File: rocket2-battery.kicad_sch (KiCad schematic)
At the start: 14 parts, among them J1 Conn_01x07, P1 PAD_SMD, P2 PAD_SMD, P3 PAD_SMD, P4 PAD_SMD

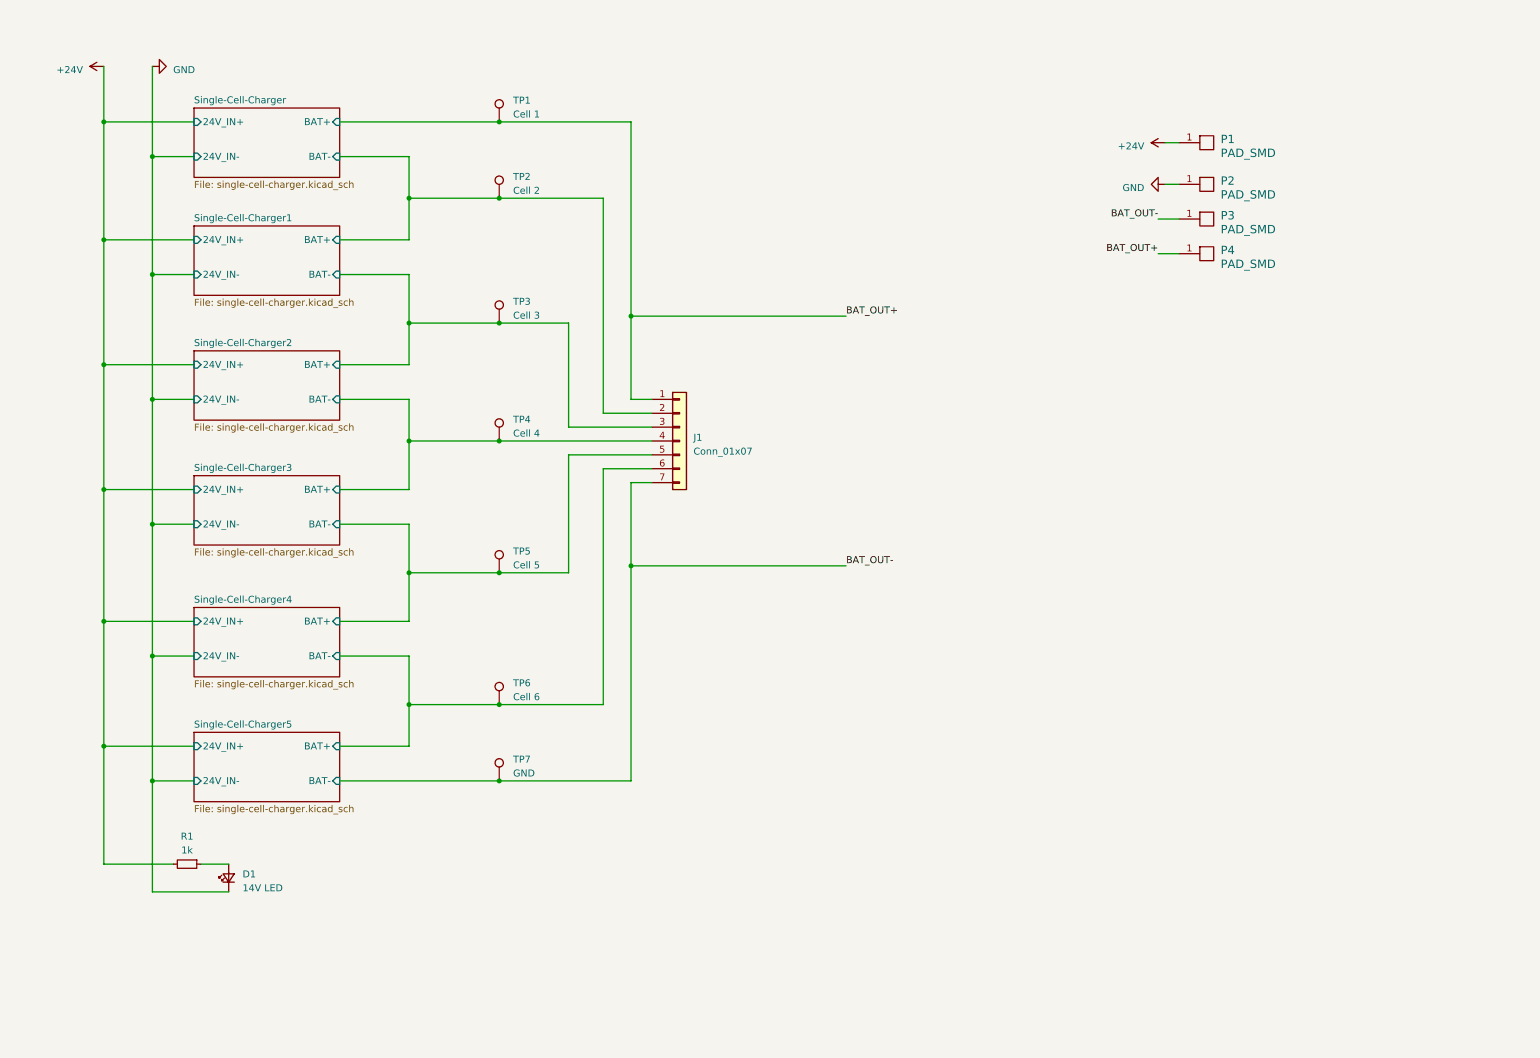
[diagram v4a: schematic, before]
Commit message: Updated schematic with symbols and footprints
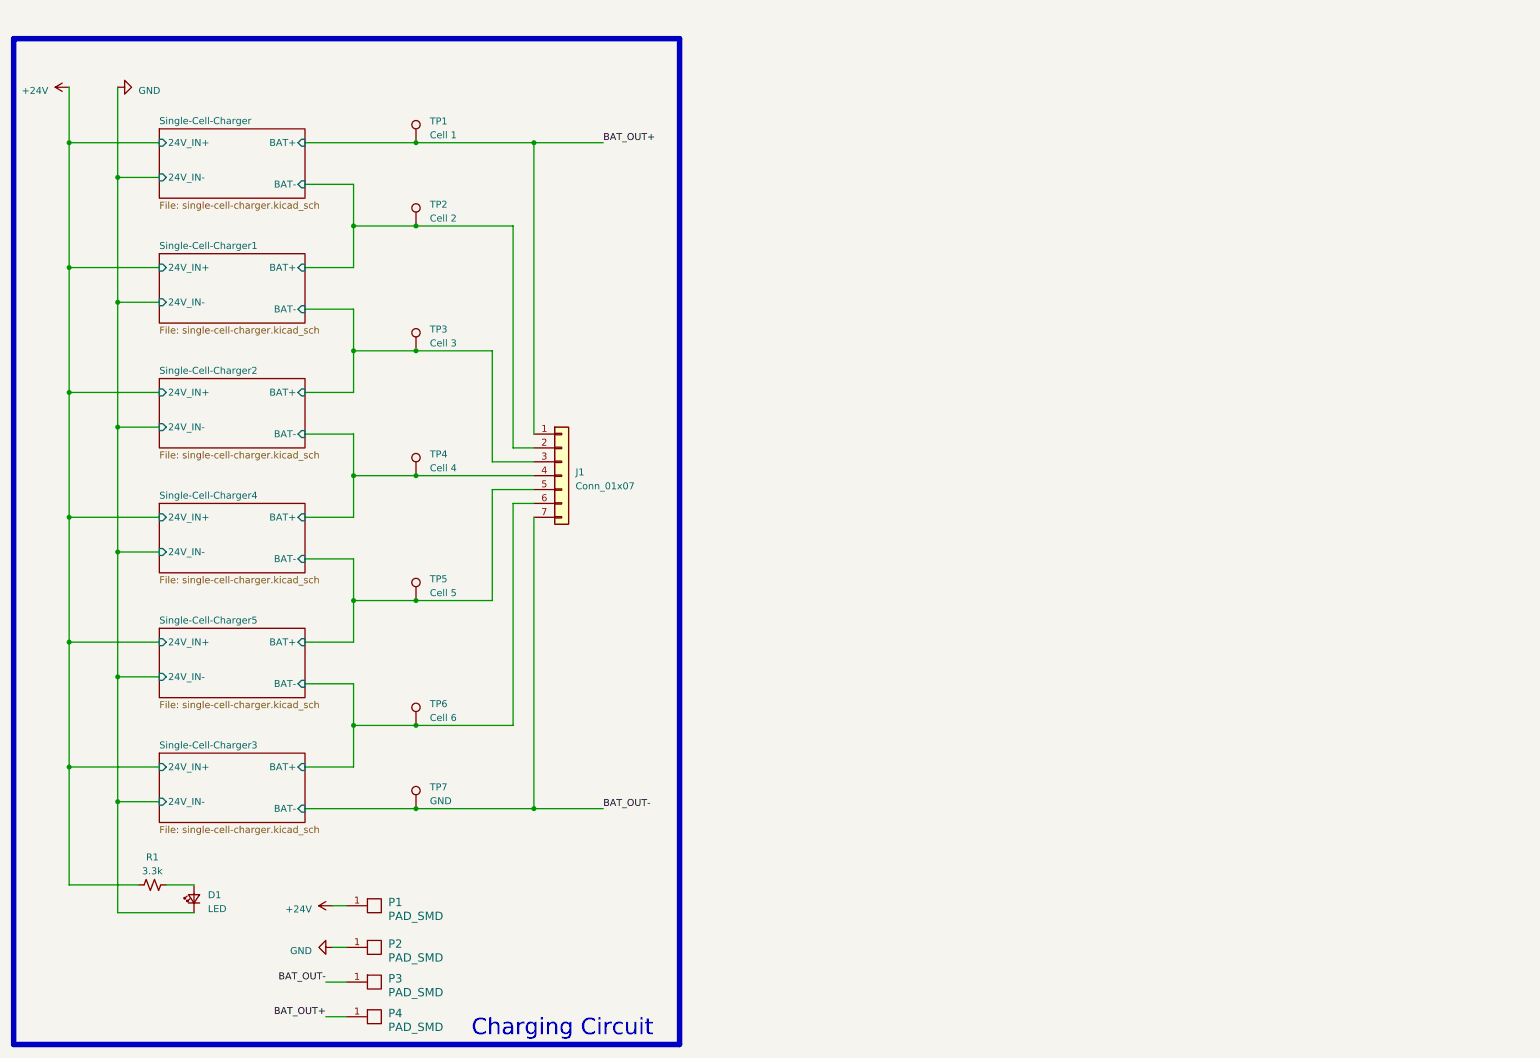
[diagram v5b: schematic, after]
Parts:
- removed R1: 1k, symbol Device:R_Small
- added R1: 3.3k, Resistor_SMD:R_0603_1608Metric_Pad0.98x0.95mm_HandSolder, symbol Device:R_Small_US
- D1: value 14V LED -> LED; footprint LED_THT:LED_D5.0mm -> LED_SMD:LED_0603_1608Metric_Pad1.05x0.95mm_HandSolder
- P1, P2, P3, P4, TP1, TP2, TP3, TP4, TP5, TP6, TP7: footprint (none) -> TestPoint:TestPoint_Pad_2.0x2.0mm
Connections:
- net Single-Cell-Charger3/BAT- is gone; now on net Single-Cell-Charger4/BAT-: J1.5 (Pin_5), TP5.1
- net +24V: now also R1.1
- net Single-Cell-Charger4/BAT-: no longer J1.6 (Pin_6), TP6.1
- net at D1.2 (A): now also R1.2
- new net Single-Cell-Charger3/BAT+: J1.6 (Pin_6), TP6.1
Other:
- note added: "Charging Circuit"
- moved on the sheet: D1, J1, P1, P2, P3, P4

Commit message: Almost done with REDs
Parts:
- added C13, C15, C16, C17, C18, C19: 100nF, Capacitor_SMD:C_0603_1608Metric, symbol Device:C_Small
- added C14: 4.7uF, Capacitor_SMD:C_0603_1608Metric, symbol Device:C_Small
- added C20: 10uF, Capacitor_SMD:C_0603_1608Metric, symbol Device:C_Small
- added C21, C22: 1uF, symbol Device:C_Small
- added D14: LED, Diode_SMD:D_0603_1608Metric, symbol Device:LED_Small
- added J2: ARM Cortex Debug, Connector_PinHeader_1.27mm:PinHeader_2x05_P1.27mm_Vertical_SMD, symbol UCIRP-KiCAD-Lib:ARM_Cortex_Debug
- added J3: SMA, Connector_Coaxial:SMA_Molex_73251-2200_Horizontal, symbol Connector:Conn_Coaxial
- added Q1, Q3, Q5, Q6: PMOS, symbol Simulation_SPICE:PMOS
- added Q2, Q4: NMOS, symbol Simulation_SPICE:NMOS
- added R38: 10K, Resistor_SMD:R_0603_1608Metric, symbol Device:R_Small_US
- added R39: 1K, Resistor_SMD:R_0603_1608Metric, symbol Device:R_Small_US
- added R40, R41, R44, R47: 100, symbol Device:R_Small_US
- added R42, R45: 1k, symbol Device:R_Small_US
- added R43, R46: 10k, symbol Device:R_Small_US
- added U2: ~, Package_QFP:LQFP-48_7x7mm_P0.5mm, symbol UCIRP-KiCAD-Lib:STM32F103C8T6
- added U4: ~, UCIRP-KiCAD-Lib:RFM95W, symbol UCIRP-KiCAD-Lib:RFM95W
- added U6: ~, Package_SO:TSOP-5_1.65x3.05mm_P0.95mm, symbol UCIRP-KiCAD-Lib:NCV8730
- added Y1: 16MHz, Crystal:Crystal_SMD_2520-4Pin_2.5x2.0mm, symbol Device:Crystal_GND24_Small
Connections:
- net BAT_OUT- is gone; now on net GND: J1.7 (Pin_7), P3.1 (PAD), TP7.1
- net +24V: now also Q1.3 (S), Q3.3 (S), R43.1
- net BAT_OUT+: now also Q5.3 (S), Q6.3 (S), R46.1
- net GND: now also C13.2, C14.2, C15.2, C16.2, C17.2, C18.2, C19.2, C20.2, C21.2, C22.2, D14.1 (K), J2.3 (GND), J2.5 (GND), J2.9 (GND_Detect), J3.2 (Ext), Q2.3 (S), Q4.3 (S), R42.1, R45.1, U2.23 (VSS), U2.35 (VSS), U2.44 (BOOT0), U2.47 (VSS), U2.8 (VSSA), U4.1 (GND), U4.10 (GND), U4.8 (GND), U6.2 (GND), Y1.2
- new net: Q4.2 (G), R44.2, R45.2
- new net: D14.2 (A), R39.2
- new net: C21.1, U6.1 (IN)
- new net: Q2.1 (D), R40.1, R43.2
- new net: Q2.2 (G), R41.2, R42.2
- new net: Q1.2 (G), Q3.2 (G), R40.2
- new net: Q5.2 (G), Q6.2 (G), R47.2
- new net: J3.1 (In), U4.9 (ANT)
- new net: Q4.1 (D), R46.2, R47.1
- new net: R39.1, U2.45 (PB8)
- new net: U2.5 (PD0), Y1.3
- new net +3.3V: C14.1, C15.1, C16.1, C17.1, C18.1, C19.1, C20.1, C22.1, J2.1 (VCC), R38.1, U2.1 (VBAT), U2.24 (VDD), U2.36 (VDD), U2.48 (VDD), U2.9 (VDDA), U4.13 (3.3V), U6.5 (OUT), Y1.4
- new net GCE+: Q1.1 (D), Q3.1 (D), Q5.1 (D), Q6.1 (D)
- new net MCU_TCK: J2.4 (SWDCLK/TCK), U2.37 (PA14)
- new net MCU_TDI: J2.8 (NC/TDI), U2.38 (PA15)
- new net MCU_TDO: J2.6 (SWO/TDO), U2.39 (PB3)
- new net MCU_TMS: J2.2 (SWDIO/TMS), U2.34 (PA13)
- new net MCU_~{RST}: C13.1, J2.10 (~{RST}), R38.2, U2.7 (~{RST})
- new net MOSFET1: R41.1, U2.10 (PA0)
- new net MOSFET2: R44.1, U2.11 (PA1)
- new net RADIO_DIO0: U2.21 (PB10), U4.14 (DIO0)
- new net RADIO_DIO1: U2.20 (PB2), U4.15 (DIO1)
- new net RADIO_DIO2: U2.19 (PB1), U4.16 (DIO2)
- new net RADIO_DIO3: U2.18 (PB0), U4.11 (DIO3)
- new net RADIO_DIO4: U2.17 (PA7), U4.12 (DIO4)
- new net RADIO_DIO5: U2.16 (PA6), U4.7 (DIO5)
- new net RADIO_MISO: U2.27 (PB14), U4.2 (MISO)
- new net RADIO_MOSI: U2.28 (PB15), U4.3 (MOSI)
- new net RADIO_SCK: U2.26 (PB13), U4.4 (SCK)
- new net RADIO_nCS: U2.25 (PB12), U4.5 (~{CS})
- new net RADIO_nRST: U2.22 (PB11), U4.6 (~{RST})
- new net V_SENSE1: U2.13 (PA3)
- new net V_SENSE2: U2.14 (PA4)
- no-connect marks 0 -> 16
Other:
- note added: "STM32 +Radio"

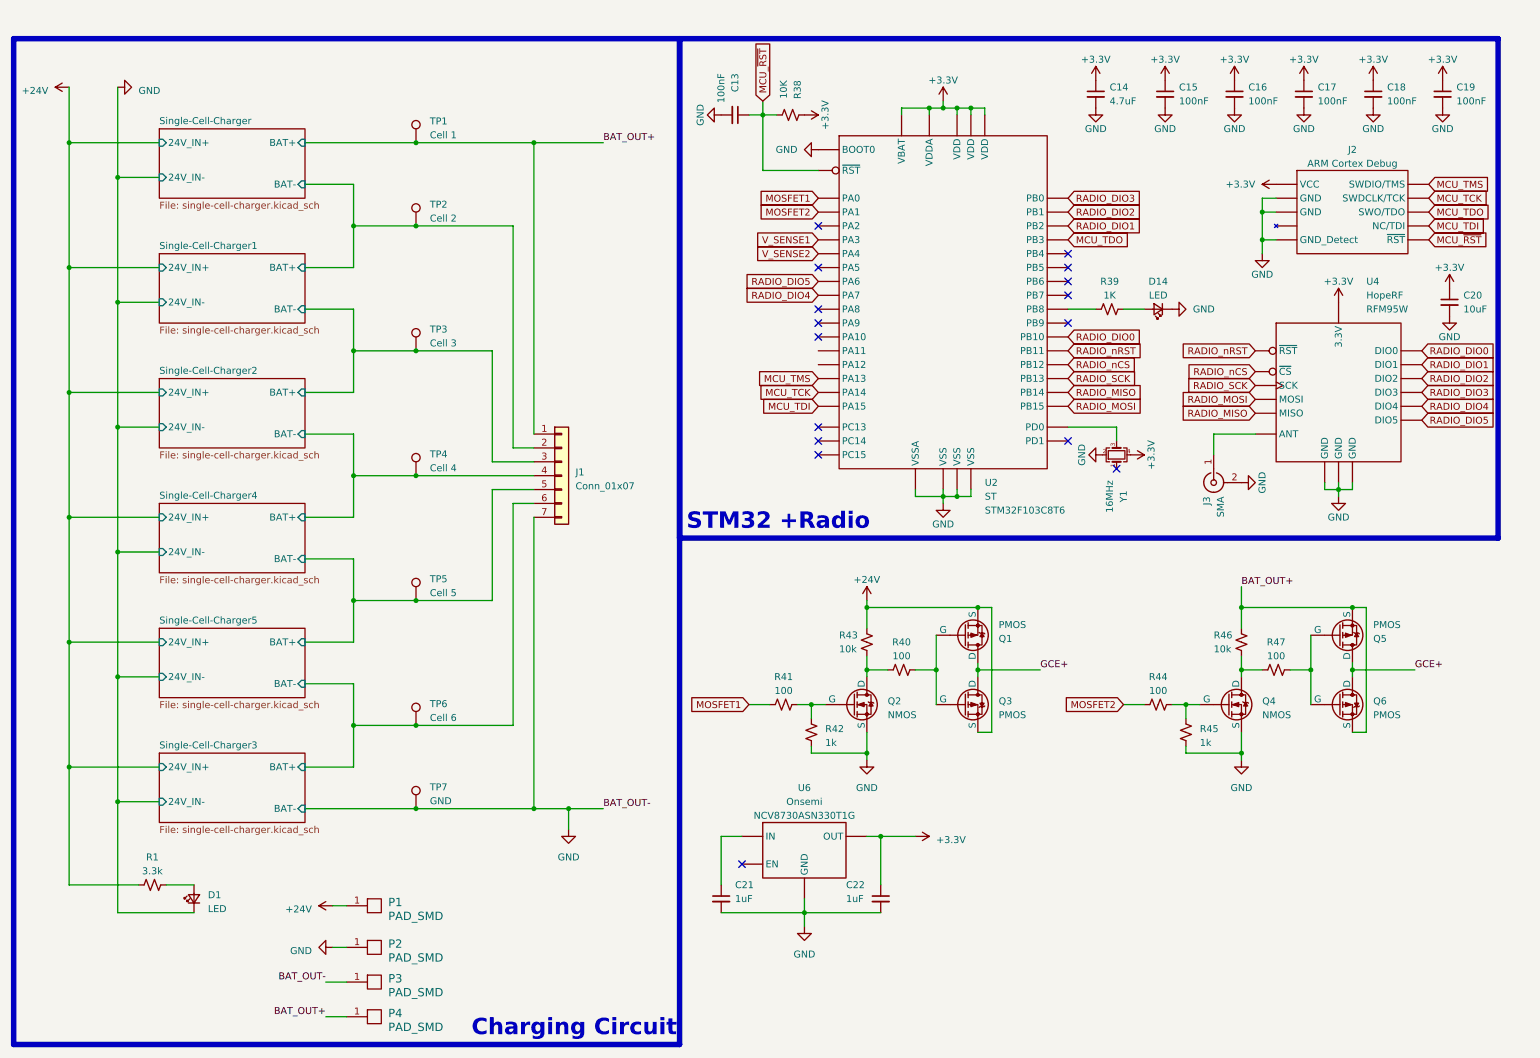
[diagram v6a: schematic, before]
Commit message: Finished Schematic; Time to Review
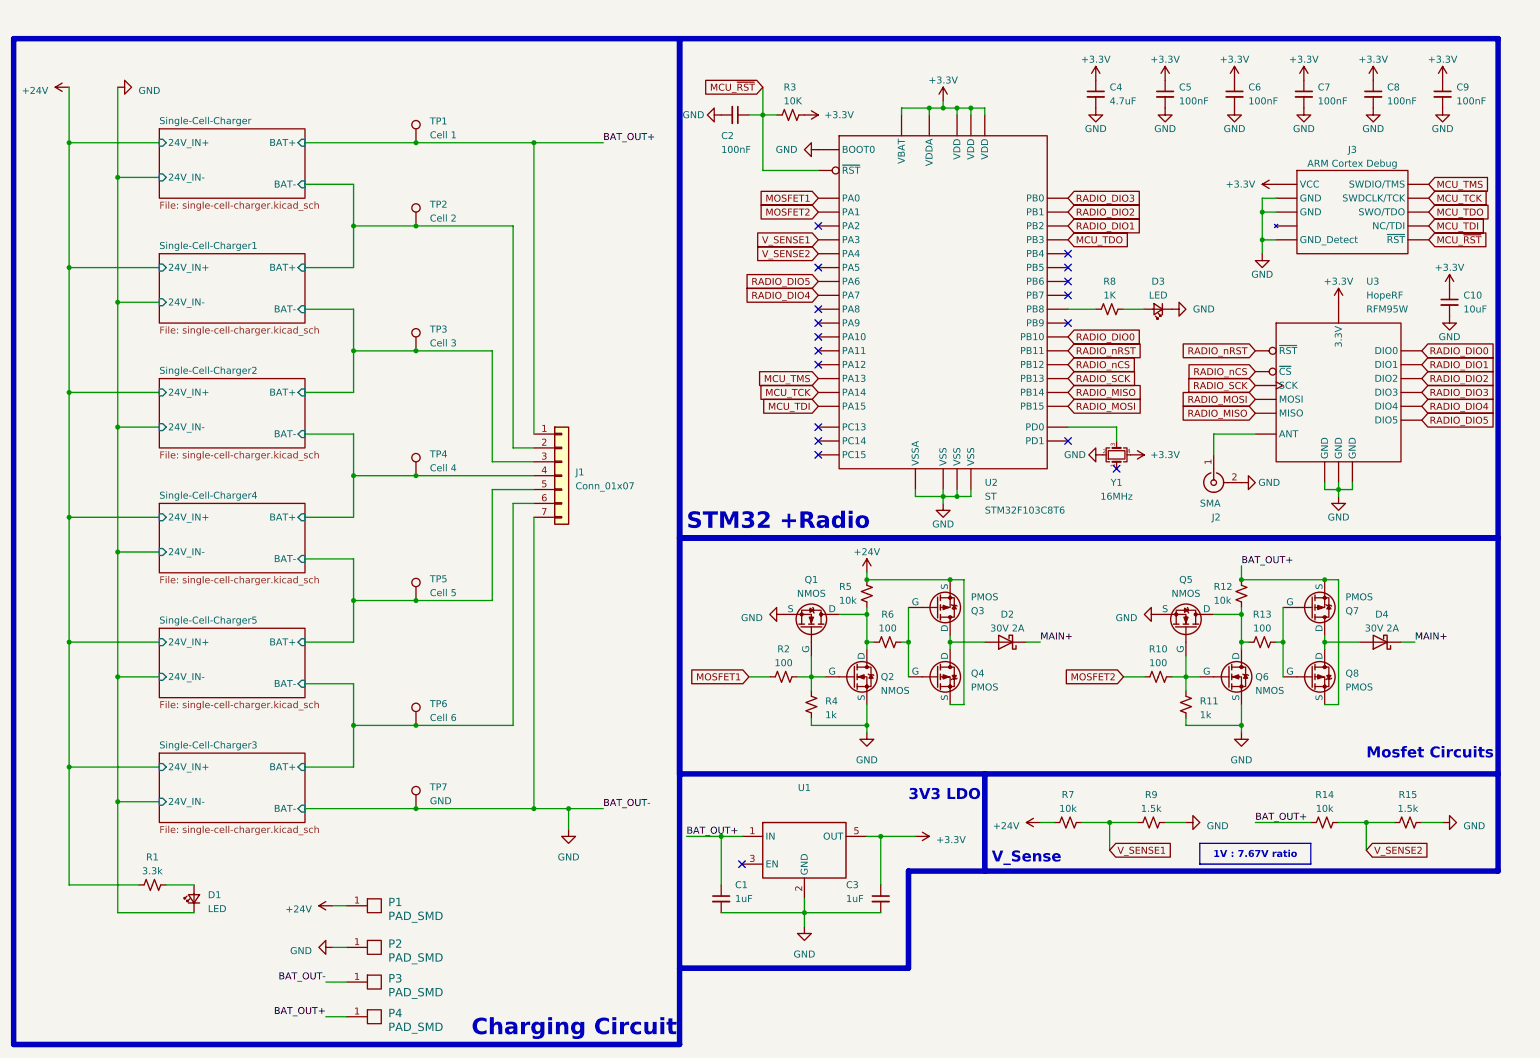
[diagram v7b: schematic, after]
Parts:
- removed Q4: NMOS, symbol Simulation_SPICE:NMOS
- removed Q5, Q6: PMOS, symbol Simulation_SPICE:PMOS
- removed R44, R47: 100, symbol Device:R_Small_US
- removed R45: 1k, symbol Device:R_Small_US
- removed R46: 10k, symbol Device:R_Small_US
- added D2, D4: 30V 2A, Diode_SMD:D_0603_1608Metric_Pad1.05x0.95mm_HandSolder, symbol Device:D_Schottky
- added Q1, Q5, Q6: NMOS, Package_TO_SOT_SMD:SOT-23-3, symbol Simulation_SPICE:NMOS
- added Q7, Q8: PMOS, Package_TO_SOT_SMD:SOT-23-3, symbol Simulation_SPICE:PMOS
- added R10, R13: 100, Resistor_SMD:R_0603_1608Metric_Pad0.98x0.95mm_HandSolder, symbol Device:R_Small_US
- added R11: 1k, Resistor_SMD:R_0603_1608Metric_Pad0.98x0.95mm_HandSolder, symbol Device:R_Small_US
- added R12, R14, R7: 10k, Resistor_SMD:R_0603_1608Metric_Pad0.98x0.95mm_HandSolder, symbol Device:R_Small_US
- added R15, R9: 1.5k, Resistor_SMD:R_0603_1608Metric_Pad0.98x0.95mm_HandSolder, symbol Device:R_Small_US
- C1: renamed from C21; footprint (none) -> Capacitor_SMD:C_0603_1608Metric_Pad1.08x0.95mm_HandSolder; Manufacturer (none) -> Generic
- C10: renamed from C20; footprint Capacitor_SMD:C_0603_1608Metric -> Capacitor_SMD:C_0603_1608Metric_Pad1.08x0.95mm_HandSolder
- C2: renamed from C13; footprint Capacitor_SMD:C_0603_1608Metric -> Capacitor_SMD:C_0603_1608Metric_Pad1.08x0.95mm_HandSolder
- C3: renamed from C22; footprint (none) -> Capacitor_SMD:C_0603_1608Metric_Pad1.08x0.95mm_HandSolder; Manufacturer (none) -> Generic
- C4: renamed from C14; footprint Capacitor_SMD:C_0603_1608Metric -> Capacitor_SMD:C_0603_1608Metric_Pad1.08x0.95mm_HandSolder
- C5: renamed from C15; footprint Capacitor_SMD:C_0603_1608Metric -> Capacitor_SMD:C_0603_1608Metric_Pad1.08x0.95mm_HandSolder
- C6: renamed from C16; footprint Capacitor_SMD:C_0603_1608Metric -> Capacitor_SMD:C_0603_1608Metric_Pad1.08x0.95mm_HandSolder
- C7: renamed from C17; footprint Capacitor_SMD:C_0603_1608Metric -> Capacitor_SMD:C_0603_1608Metric_Pad1.08x0.95mm_HandSolder
- C8: renamed from C18; footprint Capacitor_SMD:C_0603_1608Metric -> Capacitor_SMD:C_0603_1608Metric_Pad1.08x0.95mm_HandSolder
- C9: renamed from C19; footprint Capacitor_SMD:C_0603_1608Metric -> Capacitor_SMD:C_0603_1608Metric_Pad1.08x0.95mm_HandSolder
- D1, J1, P1, P2, P3, P4, R1, TP1, TP2, TP3, TP4, TP5, TP6, TP7: Manufacturer (none) -> Generic
- D3: renamed from D14; footprint Diode_SMD:D_0603_1608Metric -> Diode_SMD:D_0603_1608Metric_Pad1.05x0.95mm_HandSolder
- Q2: footprint (none) -> Package_TO_SOT_SMD:SOT-23-3; Manufacturer (none) -> Onsemi; Part # (none) -> NTR4003NT3G
- Q3: renamed from Q1; footprint (none) -> Package_TO_SOT_SMD:SOT-23-3; Manufacturer (none) -> Diodes Inc; Part # (none) -> DMP510DL-7
- Q4: renamed from Q3; footprint (none) -> Package_TO_SOT_SMD:SOT-23-3; Manufacturer (none) -> Diodes Inc; Part # (none) -> DMP510DL-7
- R2: renamed from R41; footprint (none) -> Resistor_SMD:R_0603_1608Metric_Pad0.98x0.95mm_HandSolder; Manufacturer (none) -> Generic
- R3: renamed from R38; footprint Resistor_SMD:R_0603_1608Metric -> Resistor_SMD:R_0603_1608Metric_Pad0.98x0.95mm_HandSolder
- R4: renamed from R42; footprint (none) -> Resistor_SMD:R_0603_1608Metric_Pad0.98x0.95mm_HandSolder; Manufacturer (none) -> Generic
- R5: renamed from R43; footprint (none) -> Resistor_SMD:R_0603_1608Metric_Pad0.98x0.95mm_HandSolder; Manufacturer (none) -> Generic
- R6: renamed from R40; footprint (none) -> Resistor_SMD:R_0603_1608Metric_Pad0.98x0.95mm_HandSolder; Manufacturer (none) -> Generic
- U1: renamed from U6; Manufacturer (none) -> Onsemi; Manufacturer: Onsemi -> (none); Part # (none) -> NCV8730ASN330T1G; Part #: NCV8730ASN330T1G -> (none)
- renumbered J3 to J2, J2 to J3, R39 to R8, U4 to U3
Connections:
- net +24V: now also R7.1
- net BAT_OUT+: now also C1.1, U1.1 (IN), Q7.3 (S), Q8.3 (S), R12.1, R14.1
- net GND: now also Q1.3 (S), Q5.3 (S), Q6.3 (S), R11.1, R15.2, R9.2
- net MOSFET2: now also R10.1
- net V_SENSE1: now also R7.2, R9.1
- net V_SENSE2: now also R14.2, R15.1
- net at Q2.1 (D), R5.2, R6.1: now also Q1.1 (D)
- net at Q2.2 (G), R2.2, R4.2: now also Q1.2 (G)
- net GCE+: no longer names the net of Q3.1 (D), Q4.1 (D)
- net GCE+: now also D2.2 (A)
- new net: Q5.1 (D), Q6.1 (D), R12.2, R13.1
- new net: Q5.2 (G), Q6.2 (G), R10.2, R11.2
- new net: Q7.2 (G), Q8.2 (G), R13.2
- new net: D4.2 (A), Q7.1 (D), Q8.1 (D)
- new net MAIN+: D2.1 (K), D4.1 (K)
- no-connect marks 16 -> 18
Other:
- note added: "3V3 LDO"
- note added: "Mosfet Circuits"
- note added: "V_Sense"
- title: (none) -> Battery and REDs Schematic
- moved on the sheet: Q2, Q3, Q4, R2, R4, R5, R6
